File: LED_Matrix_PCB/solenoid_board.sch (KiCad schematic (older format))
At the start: 103 parts, among them J2 MCU_LEFT_LEGS, J3 MCU_RIGHT_LEGS

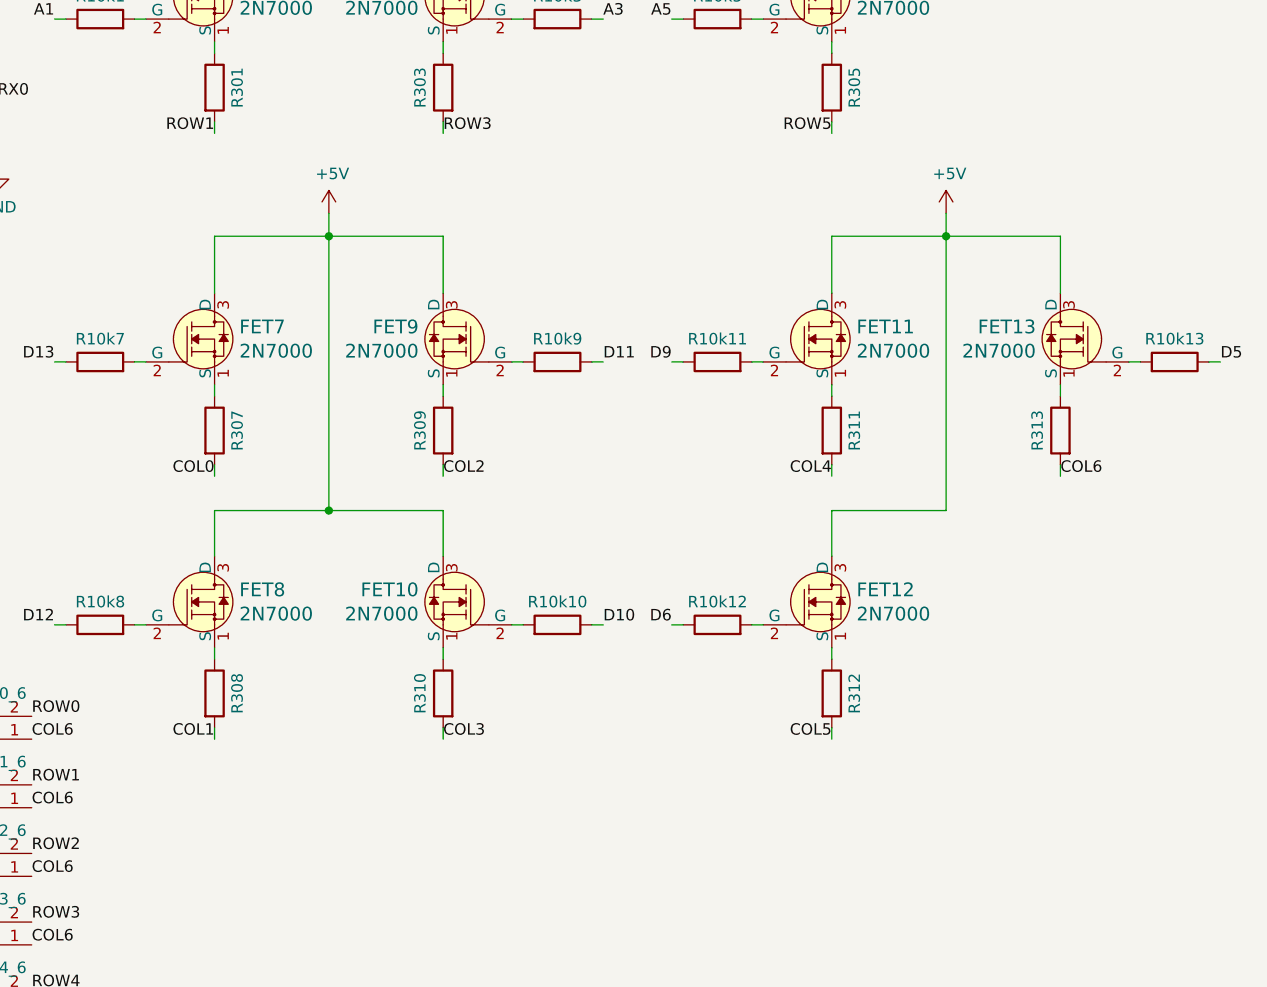
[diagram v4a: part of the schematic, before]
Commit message: Fixed the connections of the downstream MOSFETS. WOrked on geometry, sorted out footprints.
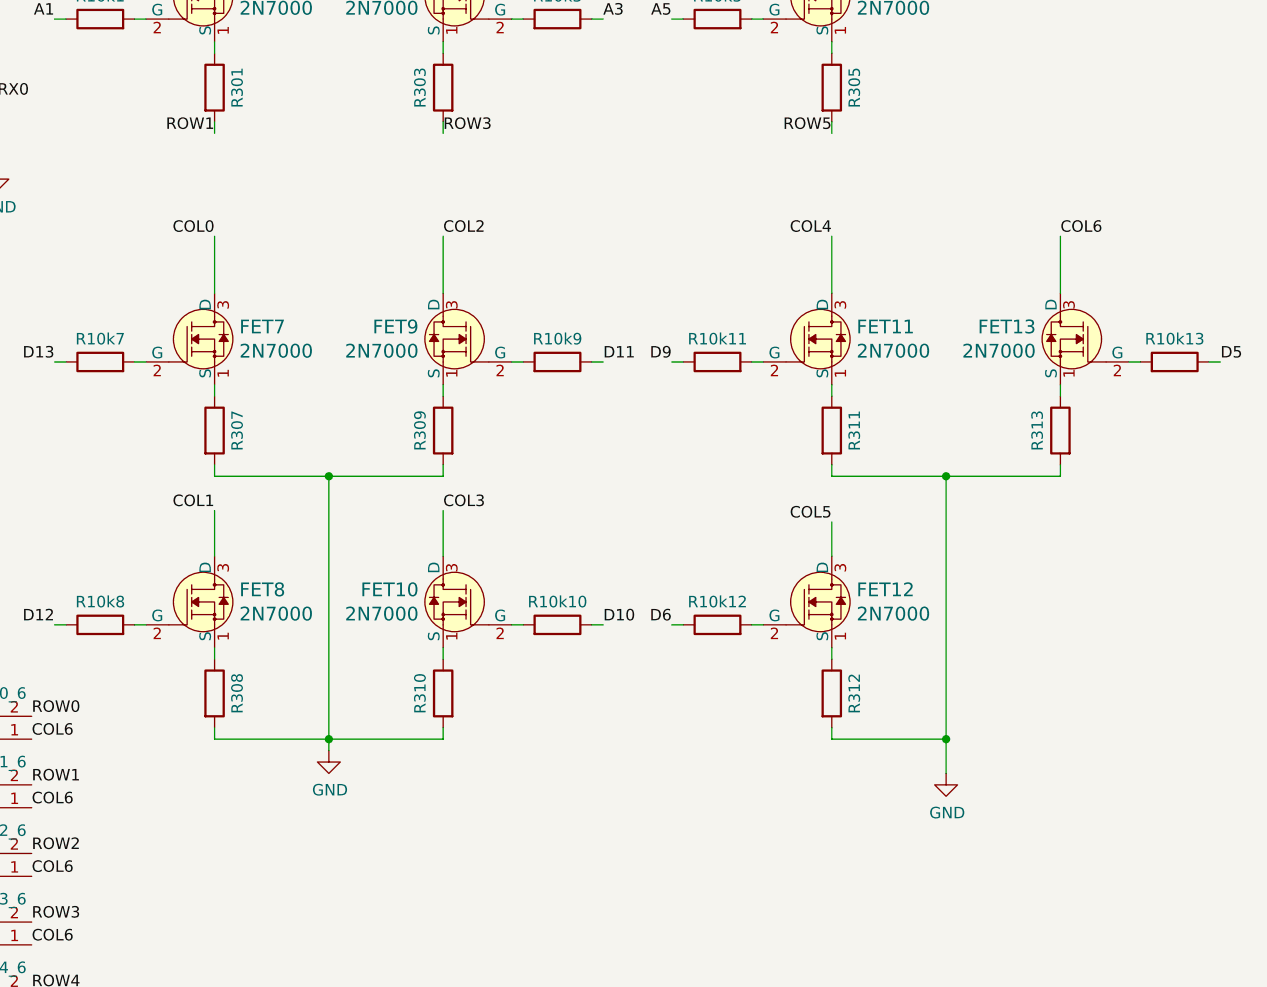
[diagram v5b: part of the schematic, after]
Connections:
- net +5V: no longer FET10.3 (D), FET11.3 (D), FET12.3 (D), FET13.3 (D), FET7.3 (D), FET8.3 (D), FET9.3 (D)
- net COL0: now also FET7.3 (D); no longer R307.2
- net COL1: now also FET8.3 (D); no longer R308.2
- net COL2: now also FET9.3 (D); no longer R309.2
- net COL3: now also FET10.3 (D); no longer R310.2
- net COL4: now also FET11.3 (D); no longer R311.2
- net COL5: now also FET12.3 (D); no longer R312.2
- net COL6: now also FET13.3 (D); no longer R313.2
- net GND: now also R307.2, R308.2, R309.2, R310.2, R311.2, R312.2, R313.2
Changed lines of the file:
@@
 Text Label 4400 4050 2    50   ~ 0
 D13
-Text Label 5100 4550 2    50   ~ 0
+Text Label 5100 3500 2    50   ~ 0
 COL0
-Text Label 5100 5700 2    50   ~ 0
+Text Label 5100 4700 2    50   ~ 0
 COL1
 $Comp
@@
 Wire Wire Line
 	4450 5200 4400 5200
-$Comp
-L power:+5V #PWR0106
-U 1 1 5E813AB9
-P 5600 3400
-F 0 "#PWR0106" H 5600 3250 50  0001 C CNN
-F 1 "+5V" H 5615 3573 50  0000 C CNN
-F 2 "" H 5600 3400 50  0001 C CNN
-F 3 "" H 5600 3400 50  0001 C CNN
-	1    5600 3400
-	1    0    0    -1
-$EndComp
-Wire Wire Line
-	5600 3500 5600 3400
 Wire Wire Line
 	5100 5300 5100 5350
@@
 Text Label 6800 4050 0    50   ~ 0
 D11
-Text Label 6100 4550 0    50   ~ 0
+Text Label 6100 3500 0    50   ~ 0
 COL2
-Text Label 6100 5700 0    50   ~ 0
+Text Label 6100 4700 0    50   ~ 0
 COL3
 $Comp
@@
 	6100 3500 6100 3750
 Wire Wire Line
-	5100 3500 5600 3500
-Wire Wire Line
 	5100 3500 5100 3750
 Wire Wire Line
-	6100 4700 5600 4700
-Wire Wire Line
 	5100 4700 5100 4900
 Wire Wire Line
 	6100 4700 6100 4900
-Wire Wire Line
-	5600 4700 5600 3500
-Connection ~ 5600 4700
-Wire Wire Line
-	5600 4700 5100 4700
-Connection ~ 5600 3500
-Wire Wire Line
-	5600 3500 6100 3500
 Text Label 7100 4050 2    50   ~ 0
 D9
-Text Label 7800 4550 2    50   ~ 0
+Text Label 7800 3500 2    50   ~ 0
 COL4
-Text Label 7800 5700 2    50   ~ 0
+Text Label 7800 4750 2    50   ~ 0
 COL5
 $Comp
@@
 Wire Wire Line
 	7150 5200 7100 5200
-$Comp
-L power:+5V #PWR0108
-U 1 1 5E813B4F
-P 8300 3400
-F 0 "#PWR0108" H 8300 3250 50  0001 C CNN
-F 1 "+5V" H 8315 3573 50  0000 C CNN
-F 2 "" H 8300 3400 50  0001 C CNN
-F 3 "" H 8300 3400 50  0001 C CNN
-	1    8300 3400
-	1    0    0    -1
-$EndComp
-Wire Wire Line
-	8300 3500 8300 3400
 Wire Wire Line
 	7800 5300 7800 5350
@@
 Text Label 9500 4050 0    50   ~ 0
 D5
-Text Label 8800 4550 0    50   ~ 0
+Text Label 8800 3500 0    50   ~ 0
 COL6
 $Comp
@@
 	8800 3500 8800 3750
 Wire Wire Line
-	7800 3500 8300 3500
-Wire Wire Line
 	7800 3500 7800 3750
-Wire Wire Line
-	7800 4700 7800 4900
-Wire Wire Line
-	8300 4700 8300 3500
-Wire Wire Line
-	8300 4700 7800 4700
-Connection ~ 8300 3500
-Wire Wire Line
-	8300 3500 8800 3500
 $Comp
 L Connector_Generic:Conn_01x01 GND1
@@
 	-1   0    0    1
 $EndComp
+$Comp
+L power:GND #PWR?
+U 1 1 5E5E78DF
+P 5600 5750
+F 0 "#PWR?" H 5600 5500 50  0001 C CNN
+F 1 "GND" H 5605 5577 50  0000 C CNN
+F 2 "" H 5600 5750 50  0001 C CNN
+F 3 "" H 5600 5750 50  0001 C CNN
+	1    5600 5750
+	1    0    0    -1
+$EndComp
+Wire Wire Line
+	6100 5700 5600 5700
+Wire Wire Line
+	5100 4550 5600 4550
+Wire Wire Line
+	5600 4550 5600 5700
+Connection ~ 5600 4550
+Wire Wire Line
+	5600 4550 6100 4550
+Connection ~ 5600 5700
+Wire Wire Line
+	5600 5700 5100 5700
+Wire Wire Line
+	5600 5750 5600 5700
+Wire Wire Line
+	7800 4900 7800 4750
+$Comp
+L power:GND #PWR?
+U 1 1 5E657BD0
+P 8300 5850
+F 0 "#PWR?" H 8300 5600 50  0001 C CNN
+F 1 "GND" H 8305 5677 50  0000 C CNN
+F 2 "" H 8300 5850 50  0001 C CNN
+F 3 "" H 8300 5850 50  0001 C CNN
+	1    8300 5850
+	1    0    0    -1
+$EndComp
+Wire Wire Line
+	7800 4550 8300 4550
+Wire Wire Line
+	7800 5700 8300 5700
+Wire Wire Line
+	8300 5700 8300 5850
+Wire Wire Line
+	8300 5700 8300 4550
+Connection ~ 8300 5700
+Connection ~ 8300 4550
+Wire Wire Line
+	8300 4550 8800 4550
 $EndSCHEMATC

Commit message: Changed mosfet circuitry.
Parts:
- removed R307, R308, R309, R310, R311, R312, R313: 300, Resistor_THT:R_Axial_DIN0204_L3.6mm_D1.6mm_P5.08mm_Vertical, symbol Device:R
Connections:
- net +5V: now also R300.1, R301.1, R302.1, R303.1, R304.1, R305.1, R306.1; no longer FET0.3 (D), FET1.3 (D), FET2.3 (D), FET3.3 (D), FET4.3 (D), FET5.3 (D), FET6.3 (D)
- net A2: no longer R10k2.1
- net GND: now also FET10.1 (S), FET11.1 (S), FET12.1 (S), FET13.1 (S), FET7.1 (S), FET8.1 (S), FET9.1 (S)
- net ROW0: now also FET0.1 (S); no longer R300.2
- net ROW1: now also FET1.1 (S); no longer R301.2
- net ROW2: now also FET2.1 (S); no longer R302.2
- net ROW3: now also FET3.1 (S); no longer R303.2
- net ROW4: now also FET4.1 (S); no longer R304.2
- net ROW5: now also FET5.1 (S); no longer R305.2
- net ROW6: now also FET6.1 (S); no longer R306.2
- new net: FET0.3 (D), R300.2
- new net: FET1.3 (D), R301.2
- new net: FET2.3 (D), R302.2
- new net: FET3.3 (D), R303.2
- new net: FET4.3 (D), R304.2
- new net: FET5.3 (D), R305.2
- new net: FET6.3 (D), R306.2
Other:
- moved on the sheet: FET0, FET1, FET2, FET3, FET4, FET5, FET6, R10k0, R10k1, R10k2, R10k3, R10k4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

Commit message: Added a pull down resistor and re-routed. Also, updated BOM.
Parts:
- added R3k0, R3k1, R3k10, R3k11, R3k12, R3k13, R3k2, R3k3, R3k4, R3k5, R3k6, R3k7, R3k8, R3k9: 3k, Resistor_THT:R_Axial_DIN0204_L3.6mm_D1.6mm_P5.08mm_Vertical, symbol Device:R
- R100: renamed from R10k0; value 10k -> 100
- R101: renamed from R10k1; value 10k -> 10
- R102: renamed from R10k2; value 10k -> 100
- R103: renamed from R10k3; value 10k -> 100
- R104: renamed from R10k4; value 10k -> 100
- R105: renamed from R10k5; value 10k -> 100
- R106: renamed from R10k6; value 10k -> 100
- R107: renamed from R10k7; value 10k -> 100
- R108: renamed from R10k8; value 10k -> 100
- R109: renamed from R10k9; value 10k -> 100
- R110: renamed from R10k10; value 10k -> 100
- R111: renamed from R10k11; value 10k -> 100
- R112: renamed from R10k12; value 10k -> 100
- R113: renamed from R10k13; value 10k -> 100
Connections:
- net A6 is gone; now on net SCK: R106.1
- net A2: now also R102.1
- net GND: now also R3k0.1, R3k1.1, R3k10.1, R3k11.1, R3k12.1, R3k13.1, R3k2.1, R3k3.1, R3k4.1, R3k5.1, R3k6.1, R3k7.1, R3k8.1, R3k9.1
- net at FET0.2 (G), R100.2: now also R3k0.2
- net at FET1.2 (G), R101.2: now also R3k1.2
- net at FET2.2 (G), R102.2: now also R3k2.2
- net at FET3.2 (G), R103.2: now also R3k3.2
- net at FET4.2 (G), R104.2: now also R3k4.2
- net at FET5.2 (G), R105.2: now also R3k5.2
- net at FET6.2 (G), R106.2: now also R3k6.2
- net at FET7.2 (G), R107.2: now also R3k7.2
- net at FET8.2 (G), R108.2: now also R3k8.2
- net at FET9.2 (G), R109.2: now also R3k9.2
- net at FET10.2 (G), R110.2: now also R3k10.2
- net at FET11.2 (G), R111.2: now also R3k11.2
- net at FET12.2 (G), R112.2: now also R3k12.2
- net at FET13.2 (G), R113.2: now also R3k13.2
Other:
- moved on the sheet: R100, R101, R102, R103, R104
